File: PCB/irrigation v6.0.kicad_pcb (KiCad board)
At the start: 6 copper layers, 90.2 x 69.8 mm, 15 parts, among them J1 Sol, J3 Valve, J4 Batt, J5 Capacitive soil sensor, J6 Valve, Q1 TIP120, SW2 flash, U2 WeMos_mini, U4 J5019, U5 CD4052B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

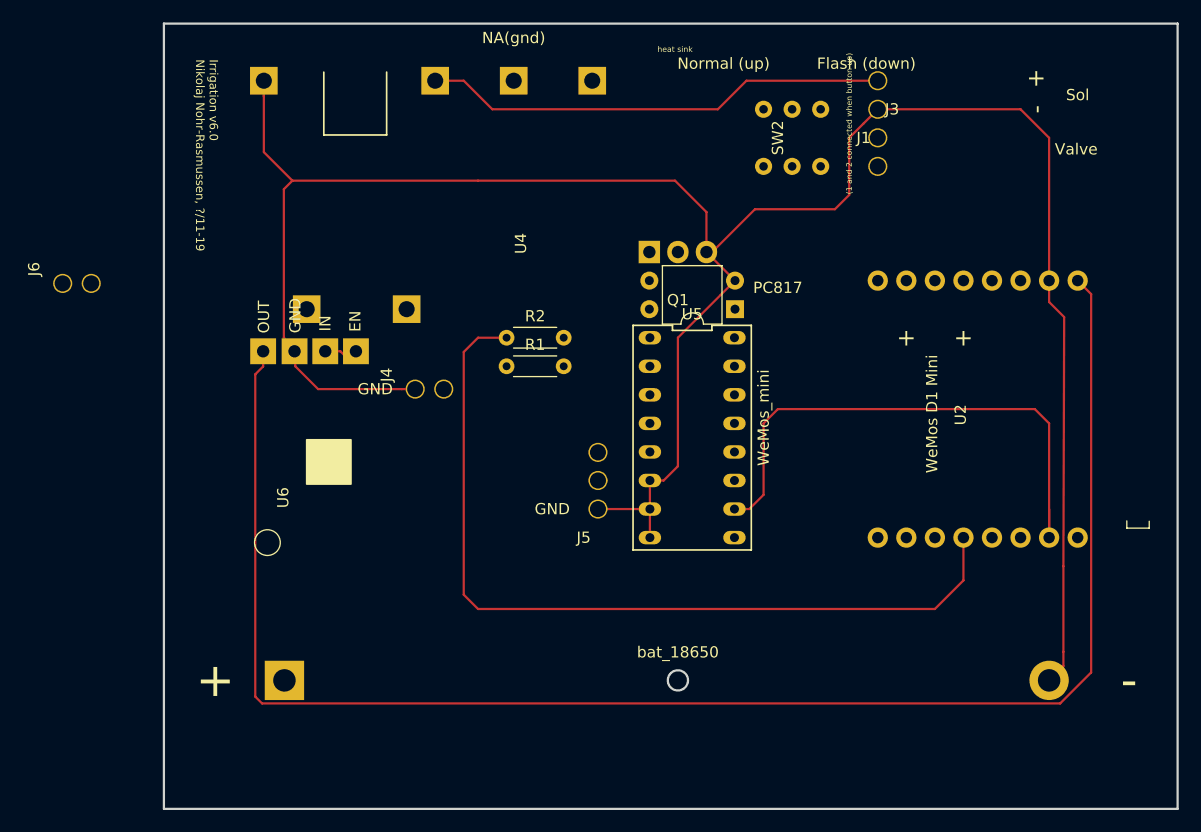
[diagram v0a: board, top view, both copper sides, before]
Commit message: Updating documentation Working on PCB board version 6.0 (only 5V and different power supply circuit)
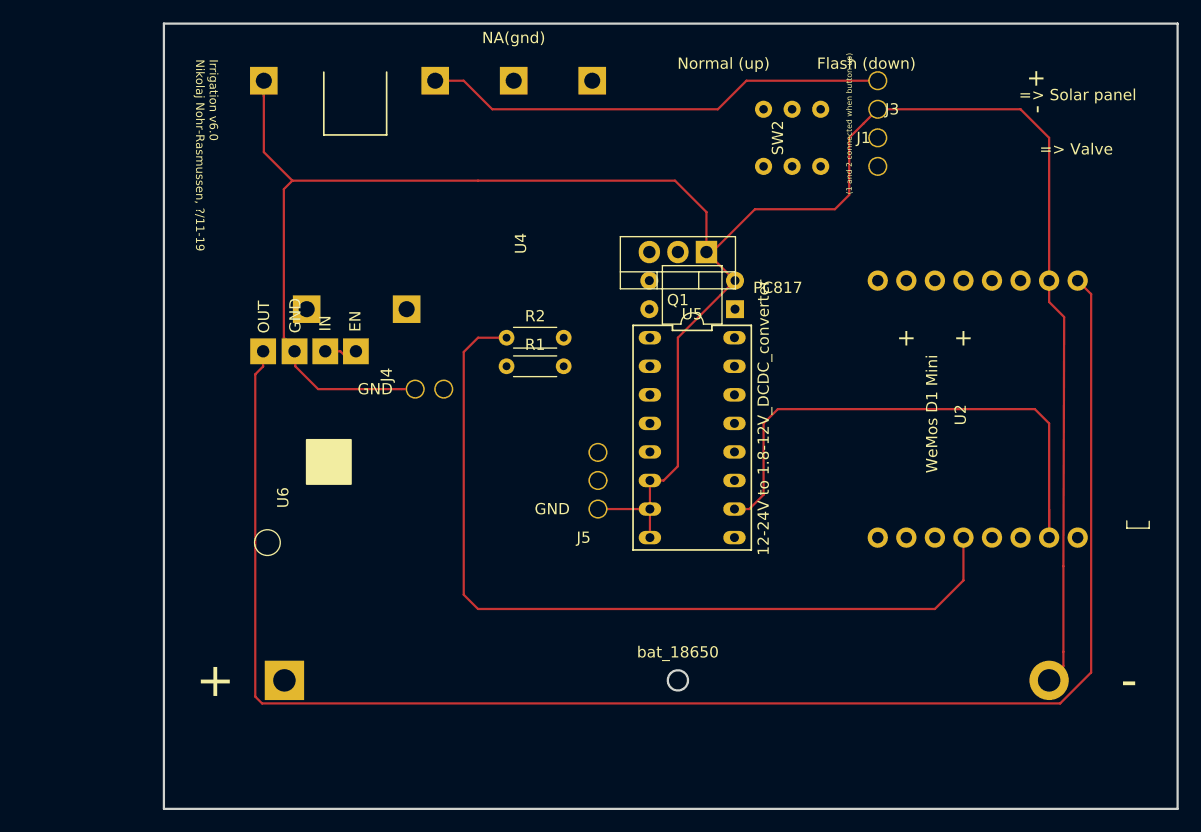
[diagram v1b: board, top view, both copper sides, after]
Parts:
- removed J6: Valve, footprint:2p_connector_v2
- J1: value Sol -> => Solar panel
- J3: value Valve -> => Valve
- J4: value Batt -> => Valve
- Q1: footprint footprint:TIP120_flat_v2 -> Package_TO_SOT_THT:TO-220-3_Vertical
- U2: value WeMos_mini -> 12-24V to 1.8-12V_DCDC_converter
- U4: value J5019 -> CD4052B
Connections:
- J1 pad 2: /4.0-7.5V -> (no net)
- J4 pad 1: GND -> (no net)
- Opto1 pad 1: Net-(Opto1-Pad1) -> (no net)
- R1 pad 1: Net-(J4-Pad2) -> (no net)
- R2 pad 1: Net-(R2-Pad1) -> (no net)
- SW2 pad 1: Net-(SW2-Pad1) -> (no net)
- SW2 pad 2: Net-(SW2-Pad2) -> (no net)
- U2 pad 10: Net-(U2-Pad10) -> (no net)
- U2 pad 11: Net-(SW2-Pad1) -> (no net)
- U2 pad 12: Net-(R2-Pad1) -> (no net)
- U2 pad 14: Net-(U2-Pad14) -> (no net)
- U2 pad 15: Net-(U2-Pad15) -> (no net)
- U2 pad 3: (no net) -> /12V
- U2 pad 4: (no net) -> /12V
- U2 pad 6: Net-(Opto1-Pad1) -> (no net)
- U2 pad 9: Net-(SW2-Pad2) -> (no net)
- U4 pad 3: Net-(J4-Pad2) -> (no net)
- U4 pad 4: /12V -> (no net)
- U4 pad 5: /4.0-7.5V -> (no net)
- U5 pad 10: Net-(U2-Pad15) -> (no net)
- U5 pad 13: Net-(U2-Pad10) -> (no net)
- U5 pad 9: Net-(U2-Pad14) -> (no net)
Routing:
- net (no net): track 0.00 -> 447.6 mm
- net Net-(SW2-Pad1): track 106.9 -> 0.00 mm
- net Net-(SW2-Pad2): track 100.3 -> 0.00 mm
- net Net-(R2-Pad1): track 75.8 -> 0.00 mm
- net Net-(U2-Pad15): track 48.6 -> 0.00 mm
- net /4.0-7.5V: track 41.5 -> 0.00 mm
- net Net-(U2-Pad14): track 30.4 -> 0.00 mm
- net Net-(U2-Pad10): track 24.7 -> 0.00 mm
- net Net-(Opto1-Pad1): track 19.6 -> 0.00 mm
